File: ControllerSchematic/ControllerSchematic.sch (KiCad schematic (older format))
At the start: 3 parts

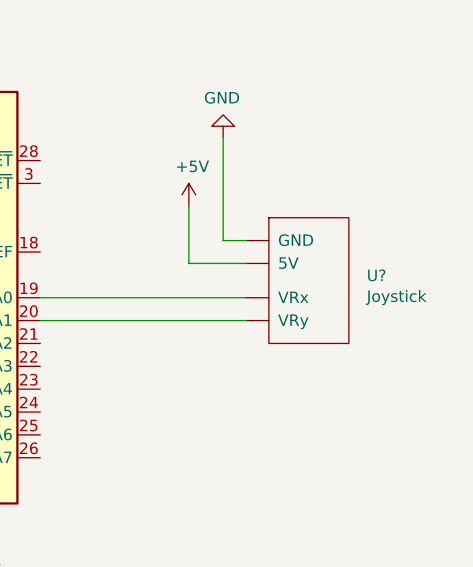
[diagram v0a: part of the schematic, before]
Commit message: Switched which Library the Joystick was in. Made no other changes.
:)
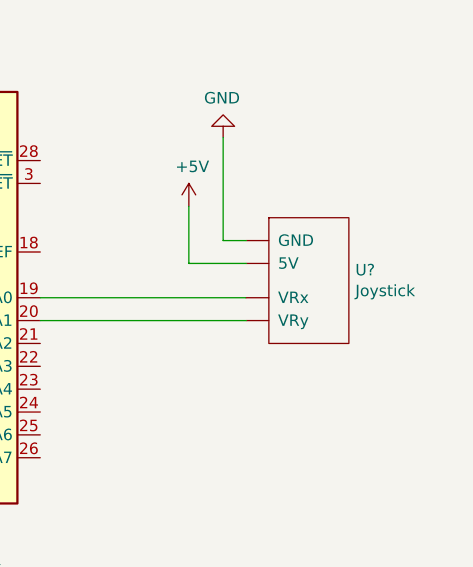
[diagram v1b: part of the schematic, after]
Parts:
- removed U?: Joystick, symbol Analog:Joystick
- added U?: Joystick, symbol NER:Joystick
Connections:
- net +5V: now also U?.~ (VRy)
- net GND: now also U?.~ (VRy)
- net at A?.19 (A0): now also U?.~ (VRy)
- net at A?.20 (A1): now also U?.~ (VRy)
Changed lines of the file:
@@
 Wire Wire Line
 	5000 2650 5000 2450
-$Comp
-L Analog:Joystick U?
-U 1 1 60B32635
-P 6450 4150
-F 0 "U?" H 6728 4746 50  0000 L CNN
-F 1 "Joystick" H 6728 4655 50  0000 L CNN
-F 2 "" H 6450 4150 50  0001 C CNN
-F 3 "" H 6450 4150 50  0001 C CNN
-	1    6450 4150
-	1    0    0    -1
-$EndComp
 Wire Wire Line
 	5300 3650 6200 3650
@@
 	-1   0    0    1
 $EndComp
+$Comp
+L NER:Joystick U?
+U 1 1 60B406FF
+P 6450 4150
+F 0 "U?" H 6678 4771 50  0000 L CNN
+F 1 "Joystick" H 6678 4680 50  0000 L CNN
+F 2 "" H 6450 4150 50  0001 C CNN
+F 3 "" H 6450 4150 50  0001 C CNN
+	1    6450 4150
+	1    0    0    -1
+$EndComp
 $EndSCHEMATC
